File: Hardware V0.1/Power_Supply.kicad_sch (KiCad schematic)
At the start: 63 parts, among them J1 ICSP, J2 Conn_01x01, J3 Conn_01x01, J4 Screw_Terminal_01x02, J6 Conn_01x04, J7 Conn_01x04, SW1 UP, SW2 DW, SW3 V_I_SEL, SW4 O_EN, U1 L78L08_SOT89, U2 ATmega328PB-AU, U3 TPS54531DDAR, U4 LM358, U5 INA138, U6 MCP4023-103ECH, Y1 16MHz

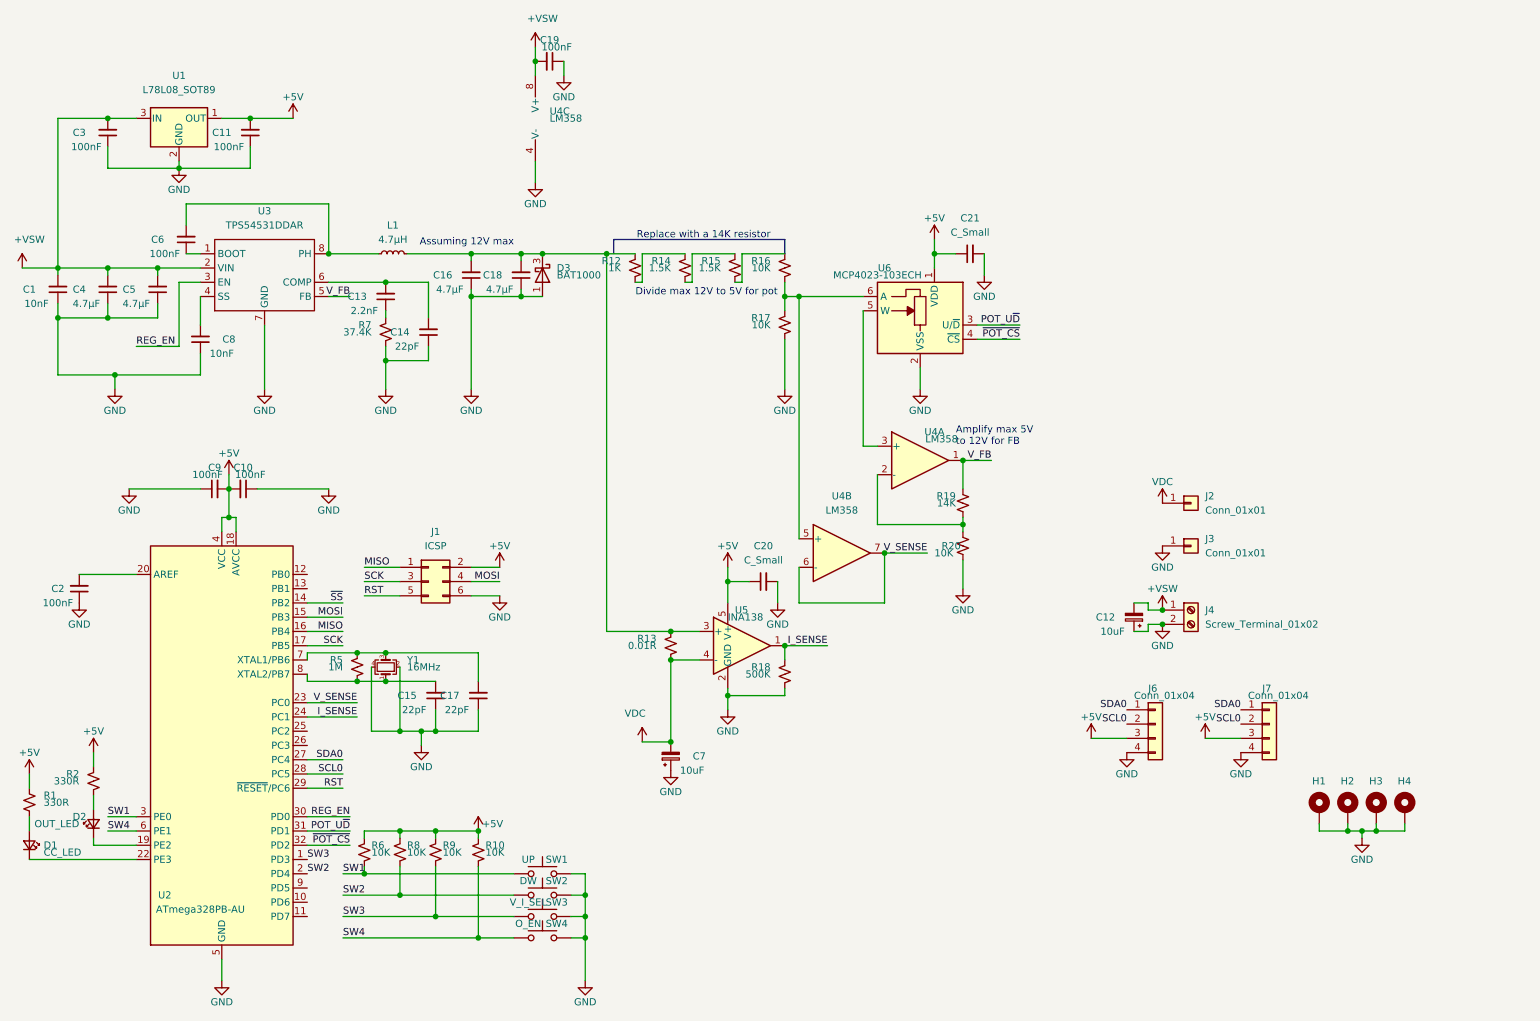
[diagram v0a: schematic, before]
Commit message: placed all components
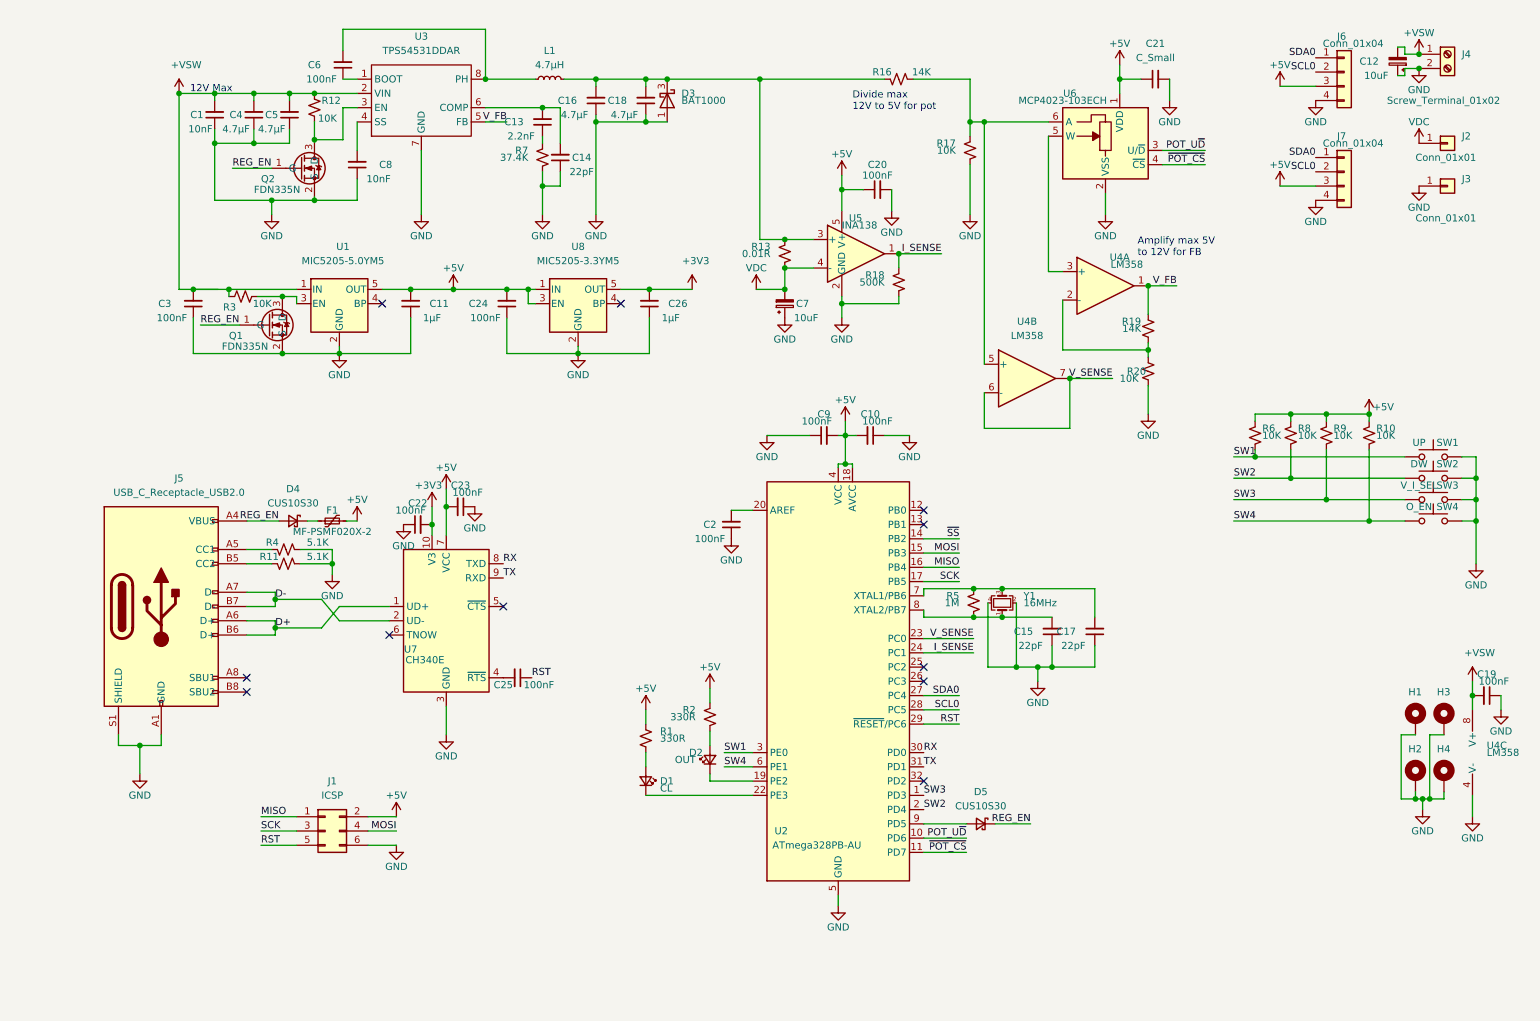
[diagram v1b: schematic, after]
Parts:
- removed R14, R15: 1.5K, Resistor_SMD:R_0805_2012Metric, symbol Device:R_Small_US
- removed U1: L78L08_SOT89, Package_TO_SOT_SMD:SOT-89-3, symbol Regulator_Linear:L78L08_SOT89
- added C22, C23, C24, C25: 100nF, Capacitor_SMD:C_0805_2012Metric, symbol Device:C_Small
- added C26: 1µF, Capacitor_SMD:C_0805_2012Metric, symbol Device:C_Small
- added D4, D5: CUS10S30, Diode_SMD:D_SOD-323, symbol Device:D_Schottky_Small
- added F1: MF-PSMF020X-2, Fuse:Fuse_0805_2012Metric_Castellated, symbol Device:Polyfuse_Small
- added J5: USB_C_Receptacle_USB2.0, Connector_USB:USB_C_Receptacle_HRO_TYPE-C-31-M-12, symbol Connector:USB_C_Receptacle_USB2.0
- added Q1, Q2: FDN335N, Package_TO_SOT_SMD:SOT-23, symbol Custom_Transistors:FDN335N
- added R11, R4: 5.1K, Resistor_SMD:R_0805_2012Metric, symbol Device:R_Small_US
- added R3: 10K, Resistor_SMD:R_0805_2012Metric, symbol Device:R_Small_US
- added U1: MIC5205-5.0YM5, Package_TO_SOT_SMD:SOT-23-5, symbol Regulator_Linear:MIC5205-5.0YM5
- added U7: CH340E, Package_SO:MSOP-10_3x3mm_P0.5mm, symbol Interface_USB:CH340E
- added U8: MIC5205-3.3YM5, Package_TO_SOT_SMD:SOT-23-5, symbol Regulator_Linear:MIC5205-3.3YM5
- C11: value 100nF -> 1µF
- C20: value C_Small -> 100nF
- D1: value CC_LED -> CL
- D2: value OUT_LED -> OUT
- R12: value 1K -> 10K
- R16: value 10K -> 14K
- U4: footprint Package_SO:SOIC-8_3.9x4.9mm_P1.27mm -> Package_SO:MSOP-8-1EP_3x3mm_P0.65mm_EP1.68x1.88mm
- Y1: footprint Crystal:Crystal_SMD_SeikoEpson_TSX3225-4Pin_3.2x2.5mm_HandSoldering -> Crystal:Crystal_SMD_SeikoEpson_TSX3225-4Pin_3.2x2.5mm
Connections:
- net +5V: now also C23.2, C24.2, F1.2, U1.5 (OUT), U7.7 (VCC), U8.1 (IN), U8.3 (EN)
- net +VSW: now also R12.2, R3.2, U1.1 (IN)
- net GND: now also C22.1, C23.1, C24.1, C26.1, J5.A1 (GND), J5.A12 (GND), J5.B1 (GND), J5.B12 (GND), J5.S1 (SHIELD), Q1.2 (S), Q2.2 (S), R11.1, R4.1, U1.2 (GND), U7.3 (GND), U8.2 (GND)
- net POT_U~D: now also U2.10 (PD6); no longer U2.31 (PD1)
- net REG_EN: now also D4.2 (A), D5.1 (K), J5.A4 (VBUS), J5.A9 (VBUS), J5.B4 (VBUS), J5.B9 (VBUS), Q1.1 (G), Q2.1 (G); no longer U2.30 (PD0), U3.3 (EN)
- net RST: now also C25.1
- net ~POT_CS: now also U2.11 (PD7); no longer U2.32 (PD2)
- net at R12.1: now also U3.3 (EN), Q2.3 (D)
- net at C16.2, C18.2, D3.3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: now also R16.2; no longer R12.2
- net at U2.9 (PD5): now also D5.2 (A)
- new net: J5.A5 (CC1), R4.2
- new net: C25.2, U7.4 (~RTS)
- new net: Q1.3 (D), R3.1, U1.3 (EN)
- new net: J5.B5 (CC2), R11.2
- new net: D4.1 (K), F1.1
- new net +3V3: C22.2, C26.2, U7.10 (V3), U8.5 (OUT)
- new net D+: J5.A6 (D+), J5.B6 (D+), U7.1 (UD+)
- new net D-: J5.A7 (D-), J5.B7 (D-), U7.2 (UD-)
- new net RX: U2.30 (PD0), U7.8 (TXD)
- new net TX: U2.31 (PD1), U7.9 (RXD)
- no-connect marks 0 -> 11
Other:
- note added: "12V Max"
- note removed: "Assuming 12V max"
- note removed: "Replace with a 14K resistor"
- moved on the sheet: C1, C10, C11, C12, C13, C14, C15, C16, C17, C18, C19, C2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

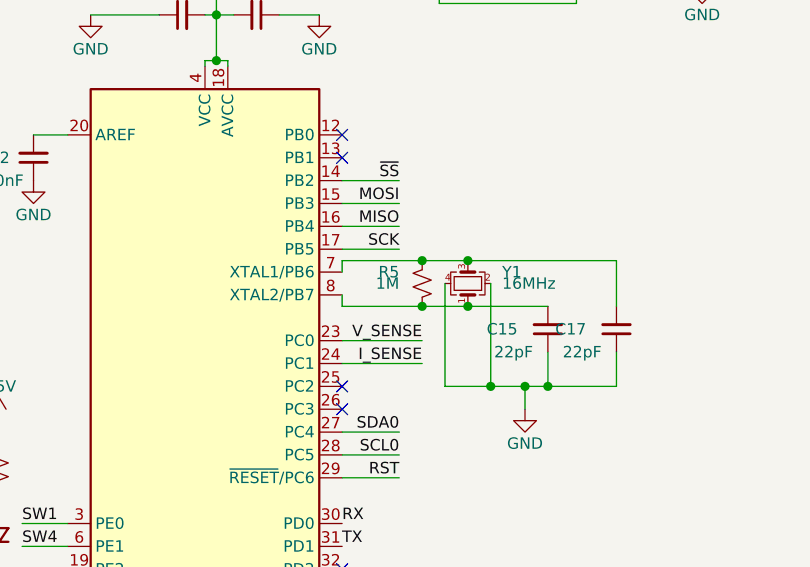
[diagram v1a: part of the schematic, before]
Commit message: schematic update-removed unnecessary resistors
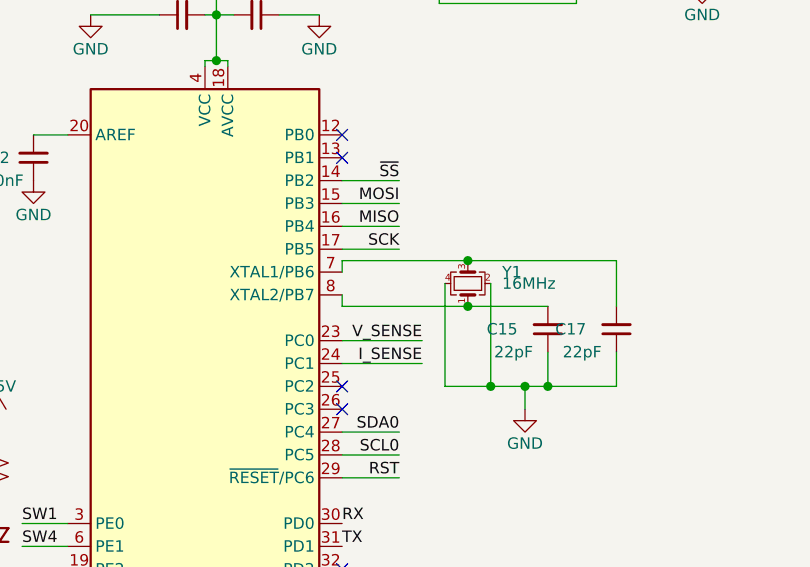
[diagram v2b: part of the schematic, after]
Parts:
- removed R5: 1M, Resistor_SMD:R_0805_2012Metric, symbol Device:R_Small_US
- J1: footprint Custom_Vertical_2x_2.54mm_Pin_Header:PinHeader_2x03_P2.54mm_Vertical -> Connector_PinSocket_1.27mm:PinSocket_2x03_P1.27mm_Vertical
- U4: footprint Package_SO:MSOP-8-1EP_3x3mm_P0.65mm_EP1.68x1.88mm -> Package_SO:MSOP-8_3x3mm_P0.65mm
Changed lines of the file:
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@@
   (junction (at 172.72 55.88) (diameter 1.016) (color 0 0 0 0))
   (junction (at 185.42 32.385) (diameter 1.016) (color 0 0 0 0))
-  (junction (at 186.055 115.57) (diameter 1.016) (color 0 0 0 0))
-  (junction (at 186.055 120.65) (diameter 1.016) (color 0 0 0 0))
   (junction (at 187.96 32.385) (diameter 1.016) (color 0 0 0 0))
   (junction (at 191.135 115.57) (diameter 1.016) (color 0 0 0 0))
@@
     (stroke (width 0) (type solid) (color 0 0 0 0))
   )
+  (wire (pts (xy 177.165 115.57) (xy 191.135 115.57))
+    (stroke (width 0) (type solid) (color 0 0 0 0))
+  )
   (wire (pts (xy 177.165 119.38) (xy 177.165 120.65))
     (stroke (width 0) (type solid) (color 0 0 0 0))
   )
-  (wire (pts (xy 177.165 120.65) (xy 186.055 120.65))
+  (wire (pts (xy 177.165 120.65) (xy 191.135 120.65))
     (stroke (width 0) (type solid) (color 0 0 0 0))
   )
@@
     (stroke (width 0) (type solid) (color 0 0 0 0))
   )
-  (wire (pts (xy 186.055 115.57) (xy 177.165 115.57))
-    (stroke (width 0) (type solid) (color 0 0 0 0))
-  )
-  (wire (pts (xy 186.055 120.65) (xy 191.135 120.65))
-    (stroke (width 0) (type solid) (color 0 0 0 0))
-  )
   (wire (pts (xy 187.96 32.385) (xy 185.42 32.385))
     (stroke (width 0) (type solid) (color 0 0 0 0))
@@
   )
   (wire (pts (xy 189.865 157.48) (xy 196.215 157.48))
-    (stroke (width 0) (type solid) (color 0 0 0 0))
-  )
-  (wire (pts (xy 191.135 115.57) (xy 186.055 115.57))
     (stroke (width 0) (type solid) (color 0 0 0 0))
   )
@@
     )
   )
-  (symbol (lib_id "Device:R_Small_US") (at 186.055 118.11 0) (mirror x) (unit 1)
-    (in_bom yes) (on_board yes)
-    (property "Reference" "R5" (id 0) (at 183.515 116.84 0)
-      (effects (font (size 1.27 1.27)) (justify right))
-    )
-    (property "Value" "1M" (id 1) (at 183.515 118.11 0)
-      (effects (font (size 1.27 1.27)) (justify right))
-    )
-    (property "Footprint" "Resistor_SMD:R_0805_2012Metric" (id 2) (at 186.055 118.11 0)
-      (effects (font (size 1.27 1.27)) hide)
-    )
-    (property "Datasheet" "~" (id 3) (at 186.055 118.11 0)
-      (effects (font (size 1.27 1.27)) hide)
-    )
-  )
   (symbol (lib_id "Device:R_Small_US") (at 217.17 69.215 0) (unit 1)
     (in_bom yes) (on_board yes)
@@
       (effects (font (size 1.27 1.27)) (justify left))
     )
-    (property "Footprint" "Package_SO:MSOP-8-1EP_3x3mm_P0.65mm_EP1.68x1.88mm" (id 2) (at 277.495 144.78 0)
+    (property "Footprint" "Package_SO:MSOP-8_3x3mm_P0.65mm" (id 2) (at 277.495 144.78 0)
       (effects (font (size 1.27 1.27)) hide)
     )
@@
     (property "Reference" "J1" (id 0) (at 71.755 149.86 0))
     (property "Value" "ICSP" (id 1) (at 71.755 152.4 0))
-    (property "Footprint" "Custom_Vertical_2x_2.54mm_Pin_Header:PinHeader_2x03_P2.54mm_Vertical" (id 2) (at 70.485 158.75 0)
+    (property "Footprint" "Connector_PinSocket_1.27mm:PinSocket_2x03_P1.27mm_Vertical" (id 2) (at 70.485 158.75 0)
       (effects (font (size 1.27 1.27)) hide)
     )
@@
     (property "Reference" "U4" (id 0) (at 195.58 67.945 0))
     (property "Value" "LM358" (id 1) (at 195.58 70.485 0))
-    (property "Footprint" "Package_SO:MSOP-8-1EP_3x3mm_P0.65mm_EP1.68x1.88mm" (id 2) (at 195.58 78.105 0)
+    (property "Footprint" "Package_SO:MSOP-8_3x3mm_P0.65mm" (id 2) (at 195.58 78.105 0)
       (effects (font (size 1.27 1.27)) hide)
     )
@@
     (property "Reference" "U4" (id 0) (at 212.09 56.515 0))
     (property "Value" "LM358" (id 1) (at 213.36 57.785 0))
-    (property "Footprint" "Package_SO:MSOP-8-1EP_3x3mm_P0.65mm_EP1.68x1.88mm" (id 2) (at 209.55 61.595 0)
+    (property "Footprint" "Package_SO:MSOP-8_3x3mm_P0.65mm" (id 2) (at 209.55 61.595 0)
       (effects (font (size 1.27 1.27)) hide)
     )
@@
       (reference "R4") (unit 1)
     )
-    (path "/da7b5872-c188-4855-8529-2397da52f80f"
-      (reference "R5") (unit 1)
-    )
     (path "/b7358b1a-38d5-41d8-bee3-4e3709bf77f3"

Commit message: finished layout for PCB with USB
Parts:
- removed J1: ICSP, Connector_PinSocket_1.27mm:PinSocket_2x03_P1.27mm_Vertical, symbol Connector_Generic:Conn_02x03_Odd_Even
- added D? (x2): CUS10S30, Diode_SMD:D_SOD-323, symbol Device:D_Schottky_Small
- added TP1, TP2, TP3, TP4, TP5, TP6: TestPoint, TestPoint:TestPoint_Pad_D1.0mm, symbol Connector:TestPoint
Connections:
- net +5V: now also D?.1 (K), D?.1 (K), TP4.1
- net GND: now also TP6.1
- net I_SENSE: now also U2.23 (PC0), D?.2 (A); no longer U2.24 (PC1)
- net MISO: now also TP1.1
- net MOSI: now also TP5.1
- net POT_U~D: now also U2.11 (PD7); no longer U2.10 (PD6)
- net RST: now also TP3.1
- net SCK: now also TP2.1
- net V_SENSE: now also U2.24 (PC1), D?.2 (A); no longer U2.23 (PC0)
- net ~POT_CS: now also U2.10 (PD6); no longer U2.11 (PD7)
